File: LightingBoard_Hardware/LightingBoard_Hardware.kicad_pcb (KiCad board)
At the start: 2 copper layers, 61 x 108.8 mm, 29 parts, among them SW1 SW_Push, SW2 SW_Push, SW3 SW_Push, U1 LDD-1500L, U2 LDD-1500L, U3 TM4C129E_Launchpad, U4 OKI

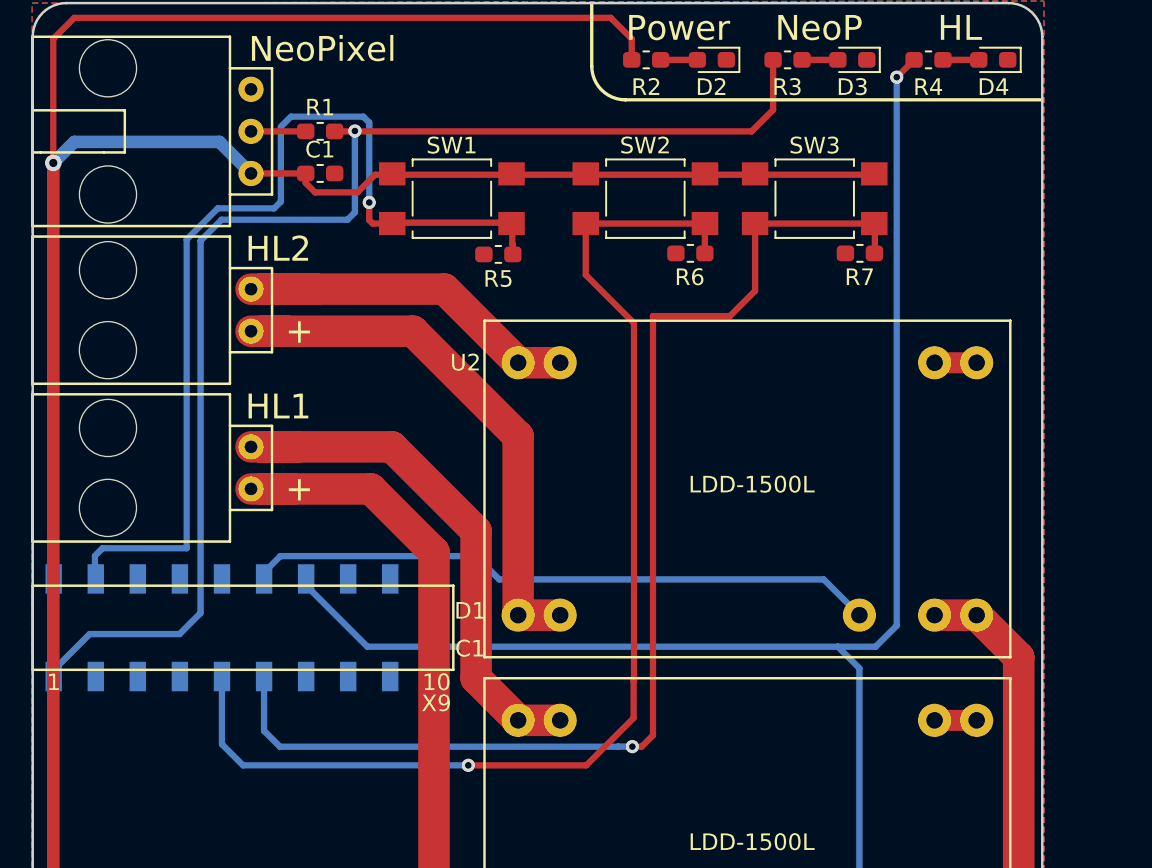
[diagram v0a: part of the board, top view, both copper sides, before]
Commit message: Added push buttons
cleaned up
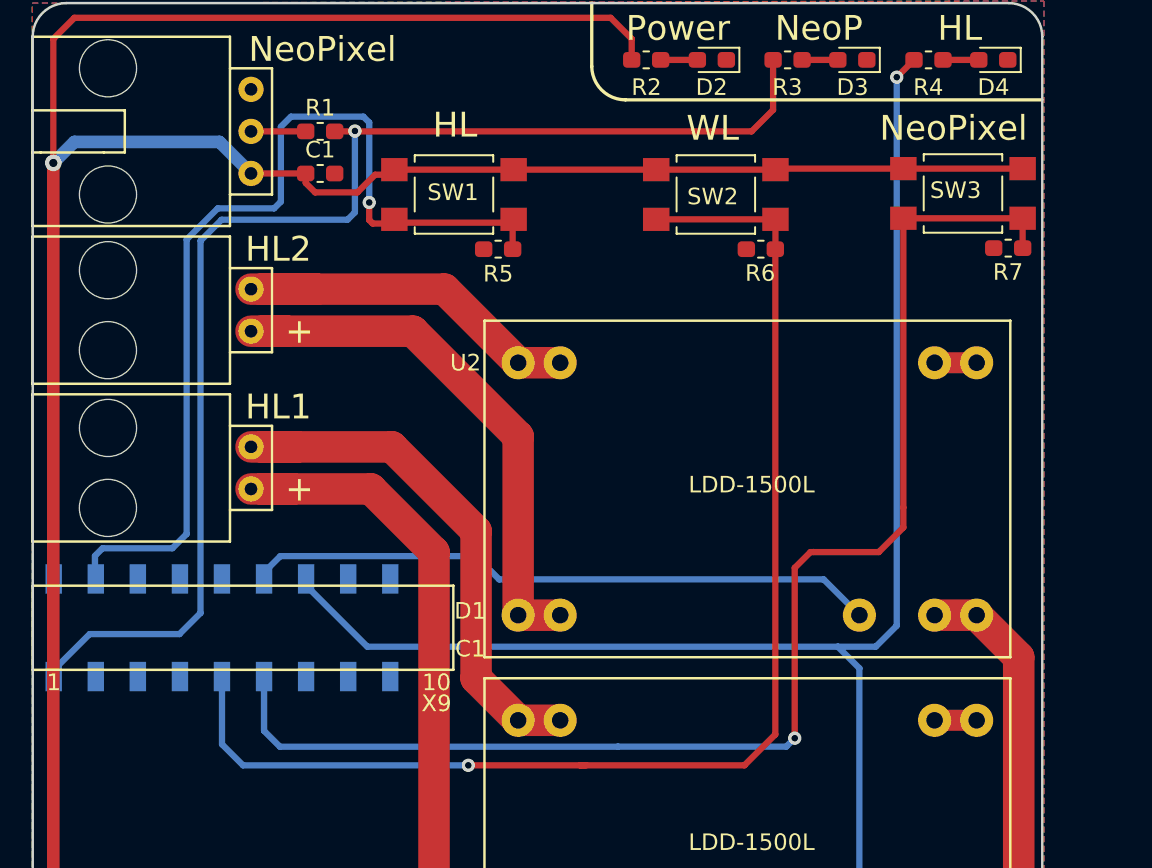
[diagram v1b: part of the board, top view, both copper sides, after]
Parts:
- moved R7 8.96 mm to (160.4, 54.9)
- moved SW3 8.96 mm to (157.7, 51.6)
- moved R6 4.26 mm to (145.5, 55.0)
- moved SW2 4.26 mm to (142.7, 51.7)
- moved R5 0.32 mm to (129.6, 55.0)
- moved SW1 0.28 mm to (126.9, 51.7)
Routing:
- net +5V: track 200.2 -> 208.9 mm
- net NeoPixel_Pattern: track 72.8 -> 81.3 mm
- net NeoPixel_White: track 70.6 -> 77.3 mm
- net Headlight_Power: track 58.7 -> 58.2 mm
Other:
- board text added: "WL"
